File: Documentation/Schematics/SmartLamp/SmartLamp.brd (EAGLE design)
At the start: 78.4 x 50.8 mm, 26 parts, among them IC1 DS3231/SO, J1 POWER_JACKPTH_BREAD, Q1 IRF1404, Q2 IRF1404, Q3 IRF1404, U1 HM-10

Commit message: Added datasheet, replaced 2.2uf cap on schematic with 100uf, to program the Tiny at 3.3v. Added Arduino communication test with HM-10 module.
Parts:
- removed C5: 0.1uF, adafruit:C025-024X044
- C3: value 0.1uF -> 100uf; device adafruit:C025-024X044 -> SparkFun-Capacitors:CPOL-RADIAL-10UF-25V
- C4: value 2.2uF -> 0.1uF; device SparkFun-Capacitors:CPOL-RADIAL-10UF-25V -> adafruit:C025-024X044
- R1, R2: device microbuilder:0805-NO -> microbuilder:_1206
- moved C3 47.5 mm to (67.3, 29.2)
- moved C4 38.1 mm to (29.2, 30.5), turned to 90 degrees
- moved C1 10.8 mm to (21.6, 16.5), turned to 270 degrees
- moved R6 1.27 mm to (38.1, 22.9)
- moved R1 0.11 mm to (29.3, 16.5)
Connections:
- net +3V3: no longer C4.1
- net GND: no longer C4.2
- net N$1: now also C4.2; no longer C5.2
- net N$2: now also C4.1; no longer C5.1
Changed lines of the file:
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@@
 <elements>
 <element name="C2" library="adafruit" package="C025-024X044" value="0.1uF" x="16.51" y="16.51" rot="R270"/>
-<element name="C4" library="SparkFun-Capacitors" package="CPOL-RADIAL-10UF-25V" value="2.2uF" x="67.31" y="29.21" rot="R270"/>
-<element name="C5" library="adafruit" package="C025-024X044" value="0.1uF" x="29.21" y="30.48" rot="R90"/>
+<element name="C3" library="SparkFun-Capacitors" package="CPOL-RADIAL-10UF-25V" value="100uf" x="67.31" y="29.21" rot="R270"/>
+<element name="C4" library="adafruit" package="C025-024X044" value="0.1uF" x="29.21" y="30.48" rot="R90"/>
 <element name="IC1" library="adafruit" package="SO16W" value="DS3231/SO" x="20.32" y="26.67"/>
 <element name="LED1" library="adafruit" package="LED3MM" value="BLUE" x="13.97" y="3.81" rot="R90"/>
@@
 </element>
 <element name="MCU1" library="SparkFun-DigitalIC" package="DIL14" value="ATTINY84ATTINY84-20PU" x="7.62" y="22.86" rot="R270"/>
-<element name="R1" library="microbuilder" package="0805-NO" value="10K" x="29.21" y="16.51" rot="R90"/>
-<element name="R2" library="microbuilder" package="0805-NO" value="10K" x="25.4" y="16.51" rot="R90"/>
-<element name="R6" library="rcl" package="0309/12" value="10K" x="39.37" y="22.86"/>
+<element name="R1" library="microbuilder" package="_1206" value="10K" x="29.3116" y="16.4719" rot="R90"/>
+<element name="R2" library="microbuilder" package="_1206" value="10K" x="25.4" y="16.51" rot="R90"/>
+<element name="R6" library="rcl" package="0309/12" value="10K" x="38.1" y="22.86"/>
 <element name="R7" library="rcl" package="0207/10" value="1K" x="38.1" y="19.05"/>
 <element name="R8" library="rcl" package="0309/12" value="470" x="24.13" y="11.43"/>
@@
 <attribute name="PROD_ID" value="PRT-10811" x="55.88" y="16.51" size="1.778" layer="27" rot="R90" display="off"/>
 </element>
-<element name="C1" library="adafruit" package="C025-024X044" value="0.1uF" x="29.21" y="24.13" rot="R90"/>
-<element name="C3" library="adafruit" package="C025-024X044" value="0.1uF" x="21.59" y="16.51" rot="R270"/>
+<element name="C1" library="adafruit" package="C025-024X044" value="0.1uF" x="21.59" y="16.51" rot="R270"/>
 <element name="BT1" library="SparkFun-Batteries" package="BATTCON_20MM_4LEGS" value="BT1" x="67.31" y="12.7" rot="R90">
 <attribute name="PROD_ID" value="BATT-10373" x="67.31" y="12.7" size="1.778" layer="27" rot="R90" display="off"/>
@@
 <contactref element="IC1" pad="9"/>
 <contactref element="LF33ABV" pad="2"/>
-<contactref element="C4" pad="2"/>
 <contactref element="IC1" pad="8"/>
 <contactref element="IC1" pad="7"/>
@@
 <contactref element="J1" pad="GND"/>
 <contactref element="C1" pad="2"/>
-<contactref element="C3" pad="2"/>
 <contactref element="IDC1" pad="8"/>
 <contactref element="IDC1" pad="10"/>
@@
 <contactref element="MCU1" pad="14"/>
 <contactref element="S1" pad="3"/>
+<contactref element="C3" pad="2"/>
 <wire x1="67.31" y1="30.48" x2="73.38" y2="43.18" width="0" layer="19" extent="1-1"/>
 <wire x1="62.23" y1="27.94" x2="67.31" y2="30.48" width="0" layer="19" extent="1-1"/>
 <wire x1="50.8" y1="27.94" x2="62.23" y2="27.94" width="0" layer="19" extent="1-1"/>
 <wire x1="39.37" y1="27.94" x2="50.8" y2="27.94" width="0" layer="19" extent="1-1"/>
-<wire x1="29.21" y1="25.4" x2="39.37" y2="27.94" width="0" layer="19" extent="1-1"/>
-<wire x1="24.765" y1="22.07" x2="29.21" y2="25.4" width="0" layer="19" extent="1-1"/>
+<wire x1="28.96" y1="36.68" x2="39.37" y2="27.94" width="0" layer="19" extent="1-1"/>
+<wire x1="26.89" y1="35.14" x2="28.96" y2="36.68" width="0" layer="19" extent="1-1"/>
+<wire x1="24.765" y1="31.27" x2="26.89" y2="35.14" width="0" layer="19" extent="1-1"/>
+<wire x1="23.495" y1="31.27" x2="24.765" y2="31.27" width="0" layer="19" extent="1-1"/>
+<wire x1="22.225" y1="31.27" x2="23.495" y2="31.27" width="0" layer="19" extent="1-1"/>
+<wire x1="20.955" y1="31.27" x2="22.225" y2="31.27" width="0" layer="19" extent="1-1"/>
+<wire x1="19.685" y1="31.27" x2="20.955" y2="31.27" width="0" layer="19" extent="1-1"/>
+<wire x1="11.43" y1="31.75" x2="19.685" y2="31.27" width="0" layer="19" extent="1-1"/>
+<wire x1="24.765" y1="22.07" x2="24.765" y2="31.27" width="0" layer="19" extent="1-1"/>
 <wire x1="23.495" y1="22.07" x2="24.765" y2="22.07" width="0" layer="19" extent="1-1"/>
 <wire x1="22.225" y1="22.07" x2="23.495" y2="22.07" width="0" layer="19" extent="1-1"/>
@@
 <wire x1="21.59" y1="15.24" x2="22.225" y2="22.07" width="0" layer="19" extent="1-1"/>
 <wire x1="16.51" y1="15.24" x2="21.59" y2="15.24" width="0" layer="19" extent="1-1"/>
-<wire x1="24.765" y1="31.27" x2="29.21" y2="25.4" width="0" layer="19" extent="1-1"/>
-<wire x1="23.495" y1="31.27" x2="24.765" y2="31.27" width="0" layer="19" extent="1-1"/>
-<wire x1="22.225" y1="31.27" x2="23.495" y2="31.27" width="0" layer="19" extent="1-1"/>
-<wire x1="20.955" y1="31.27" x2="22.225" y2="31.27" width="0" layer="19" extent="1-1"/>
-<wire x1="19.685" y1="31.27" x2="20.955" y2="31.27" width="0" layer="19" extent="1-1"/>
-<wire x1="26.89" y1="35.14" x2="24.765" y2="31.27" width="0" layer="19" extent="1-1"/>
-<wire x1="28.96" y1="36.68" x2="26.89" y2="35.14" width="0" layer="19" extent="1-1"/>
-<wire x1="11.43" y1="31.75" x2="19.685" y2="31.27" width="0" layer="19" extent="1-1"/>
 <wire x1="13.97" y1="5.08" x2="16.51" y2="15.24" width="0" layer="19" extent="1-1"/>
 <wire x1="5.08" y1="2.05" x2="13.97" y2="5.08" width="0" layer="19" extent="1-1"/>
@@
 <contactref element="MCU1" pad="12"/>
 <wire x1="11.43" y1="26.67" x2="17.145" y2="31.27" width="0" layer="19" extent="1-1"/>
-<wire x1="29.21" y1="17.46" x2="17.145" y2="31.27" width="0" layer="19" extent="1-1"/>
+<wire x1="29.3116" y1="17.7419" x2="17.145" y2="31.27" width="0" layer="19" extent="1-1"/>
 </signal>
 <signal name="SCL">
@@
 <contactref element="MCU1" pad="13"/>
 <wire x1="11.43" y1="29.21" x2="15.875" y2="31.27" width="0" layer="19" extent="1-1"/>
-<wire x1="25.4" y1="17.46" x2="15.875" y2="31.27" width="0" layer="19" extent="1-1"/>
+<wire x1="25.4" y1="17.78" x2="15.875" y2="31.27" width="0" layer="19" extent="1-1"/>
 </signal>
 <signal name="3V3" class="2">
@@
 <contactref element="R6" pad="2"/>
 <contactref element="IDC1" pad="5"/>
-<wire x1="27.94" y1="3.81" x2="45.72" y2="22.86" width="0" layer="19" extent="1-1"/>
+<wire x1="27.94" y1="3.81" x2="44.45" y2="22.86" width="0" layer="19" extent="1-1"/>
 <wire x1="3.81" y1="24.13" x2="27.94" y2="3.81" width="0" layer="19" extent="1-1"/>
 </signal>
@@
 <signal name="N$1">
 <contactref element="U1" pad="12"/>
-<contactref element="C5" pad="2"/>
+<contactref element="C4" pad="2"/>
 <wire x1="25.39" y1="35.14" x2="29.21" y2="31.75" width="0" layer="19" extent="1-1"/>
 </signal>
 <signal name="N$2">
 <contactref element="S1" pad="4"/>
-<contactref element="C5" pad="1"/>
+<contactref element="C4" pad="1"/>
 <wire x1="7.62" y1="2.05" x2="29.21" y2="29.21" width="0" layer="19" extent="1-1"/>
 </signal>
@@
 <contactref element="R6" pad="1"/>
 <contactref element="IC1" pad="2"/>
-<contactref element="C3" pad="1"/>
+<contactref element="C1" pad="1"/>
 <contactref element="R2" pad="1"/>
 <contactref element="R1" pad="1"/>
 <contactref element="LF33ABV" pad="3"/>
-<contactref element="C4" pad="1"/>
-<contactref element="C1" pad="1"/>
 <contactref element="R7" pad="1"/>
 <contactref element="S1" pad="1"/>
+<contactref element="C3" pad="1"/>
 <wire x1="53.34" y1="3.9878" x2="67.31" y2="27.94" width="0" layer="19" extent="1-1"/>
 <wire x1="33.02" y1="19.05" x2="53.34" y2="3.9878" width="0" layer="19" extent="1-1"/>
-<wire x1="33.02" y1="22.86" x2="33.02" y2="19.05" width="0" layer="19" extent="1-1"/>
-<wire x1="29.21" y1="22.86" x2="33.02" y2="22.86" width="0" layer="19" extent="1-1"/>
-<wire x1="29.21" y1="15.56" x2="33.02" y2="19.05" width="0" layer="19" extent="1-1"/>
-<wire x1="25.4" y1="15.56" x2="29.21" y2="15.56" width="0" layer="19" extent="1-1"/>
-<wire x1="21.59" y1="17.78" x2="25.4" y2="15.56" width="0" layer="19" extent="1-1"/>
+<wire x1="31.75" y1="22.86" x2="33.02" y2="19.05" width="0" layer="19" extent="1-1"/>
+<wire x1="29.3116" y1="15.2019" x2="33.02" y2="19.05" width="0" layer="19" extent="1-1"/>
+<wire x1="25.4" y1="15.24" x2="29.3116" y2="15.2019" width="0" layer="19" extent="1-1"/>
+<wire x1="21.59" y1="17.78" x2="25.4" y2="15.24" width="0" layer="19" extent="1-1"/>
 <wire x1="17.145" y1="22.07" x2="21.59" y2="17.78" width="0" layer="19" extent="1-1"/>
 <wire x1="7.62" y1="10.65" x2="17.145" y2="22.07" width="0" layer="19" extent="1-1"/>

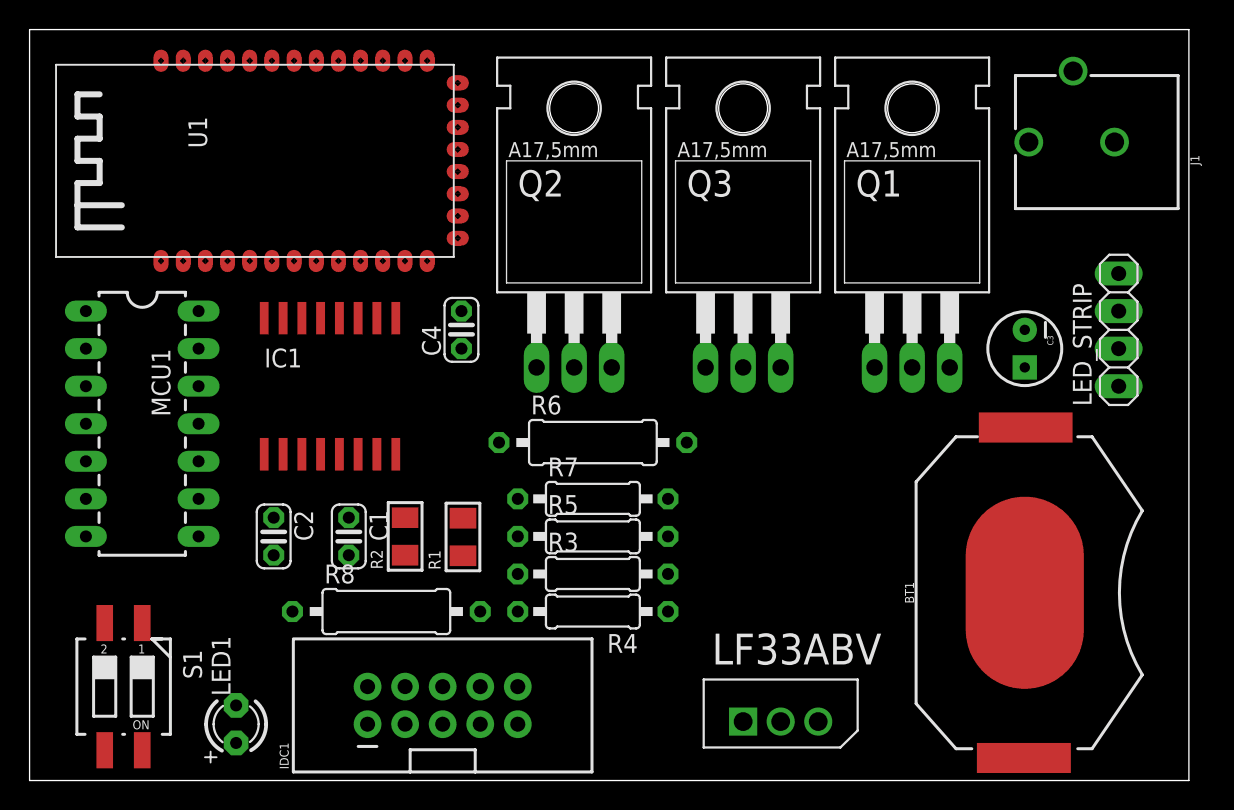
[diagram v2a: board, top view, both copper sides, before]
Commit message: Replaced SMD resistors with TH, for this version of the board.
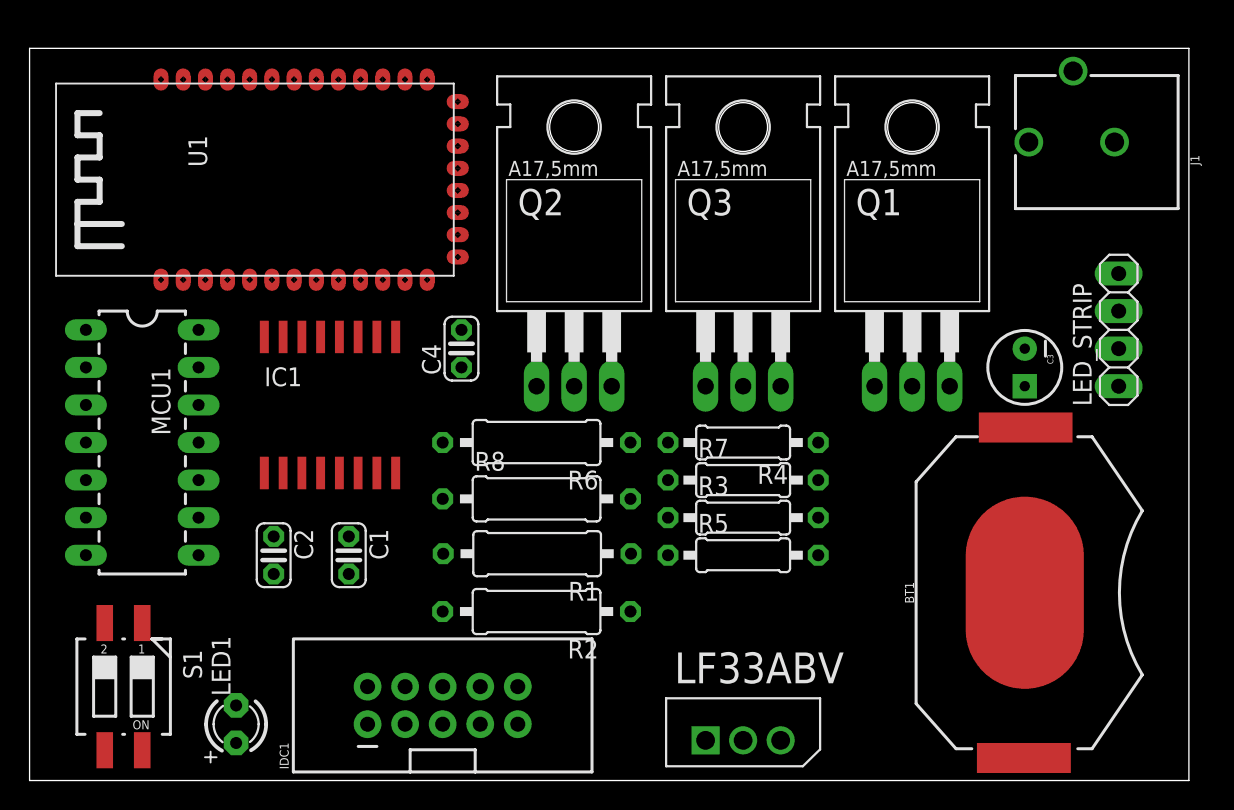
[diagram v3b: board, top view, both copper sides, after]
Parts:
- R1, R2: device microbuilder:_1206 -> rcl:0309/12
- moved R4 15.3 mm to (48.3, 22.9)
- moved R8 12.7 mm to (34.3, 19.1)
- moved R3 10.9 mm to (48.3, 17.8)
- moved R2 10.2 mm to (34.3, 11.4), turned to 180 degrees
- moved R5 10.2 mm to (48.3, 15.2)
- moved R7 10.2 mm to (48.3, 20.3)
- moved R1 5.14 mm to (34.3, 15.3), turned to 180 degrees
- moved R6 3.81 mm to (34.3, 22.9), turned to 180 degrees
- moved LF33ABV 2.84 mm to (50.8, 3.81)
- moved IC1 1.27 mm to (20.3, 25.4)
- moved C1 1.27 mm to (21.6, 15.2)
- moved C2 1.27 mm to (16.5, 15.2)
- moved C3 1.27 mm to (67.3, 27.9)
- moved C4 1.27 mm to (29.2, 29.2)
- moved MCU1 1.27 mm to (7.62, 21.6)
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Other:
- board size 78.4 x 50.8 mm -> 78.4 x 49.5 mm

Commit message: Replaced RTC device, battery holder and switch, parts to buy..
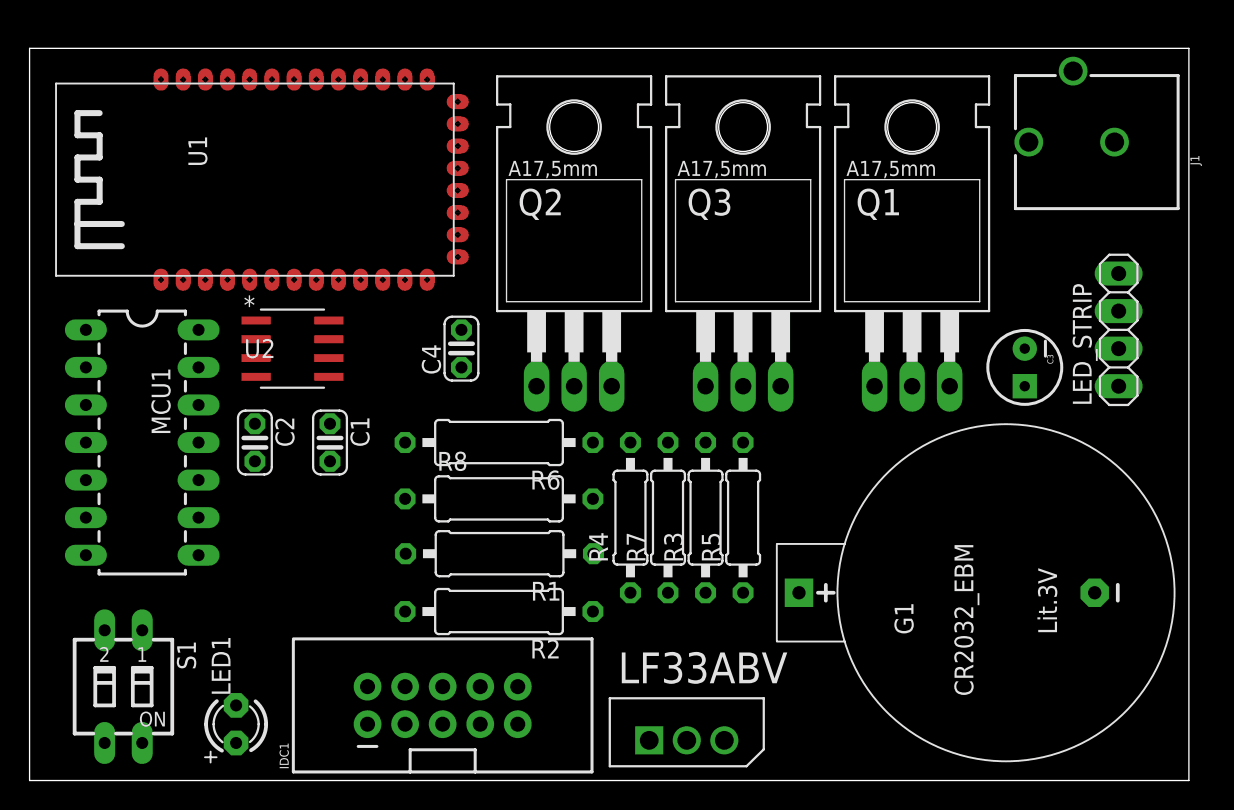
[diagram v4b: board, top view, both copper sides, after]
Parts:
- removed BT1: BT1, SparkFun-Batteries:BATTCON_20MM_4LEGS
- removed IC1: DS3231/SO, adafruit:SO16W
- added G1: CR2032_EBM, CuSTOM_GB:CR2032_EBM
- added U2: DS3231MZ, Maxim_RTC:21-0041B_8
- LED1: value BLUE -> GREEN
- S1: value 219-02 -> S1; device switch-dil:CTS-219-02 -> switch-dil:SD4-02
- moved R4 9.16 mm to (40.6, 17.8), turned to 90 degrees
- moved C2 7.73 mm to (15.2, 22.9)
- moved C1 7.73 mm to (20.3, 22.9)
- moved R7 5.68 mm to (43.2, 17.8), turned to 90 degrees
- moved LF33ABV 3.81 mm to (47.0, 3.81)
- moved R5 2.54 mm to (48.3, 17.8), turned to 90 degrees
- moved R1 2.54 mm to (31.8, 15.3)
- moved R2 2.54 mm to (31.8, 11.4)
- moved R3 2.54 mm to (45.7, 17.8), turned to 90 degrees
- moved R6 2.54 mm to (31.8, 22.9)
- moved R8 2.54 mm to (31.8, 19.1)
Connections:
- net !INT_SQW: now also U2.3; no longer IC1.3
- net +3V3: now also U2.2; no longer IC1.2
- net GND: now also G1.-, U2.5; no longer BT1.NEGATIVE, IC1.10, IC1.11, IC1.12, IC1.13, IC1.5, IC1.6, IC1.7, IC1.8, IC1.9
- net SCL: now also U2.8; no longer IC1.16
- net SDA: now also U2.7; no longer IC1.15
- net VBAT: now also G1.+, U2.6; no longer BT1.POSITIVE@1, BT1.POSITIVE@2, BT1.POSITIVE@3, BT1.POSITIVE@4, IC1.14
